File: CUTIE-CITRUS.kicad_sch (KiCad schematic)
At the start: 17 parts

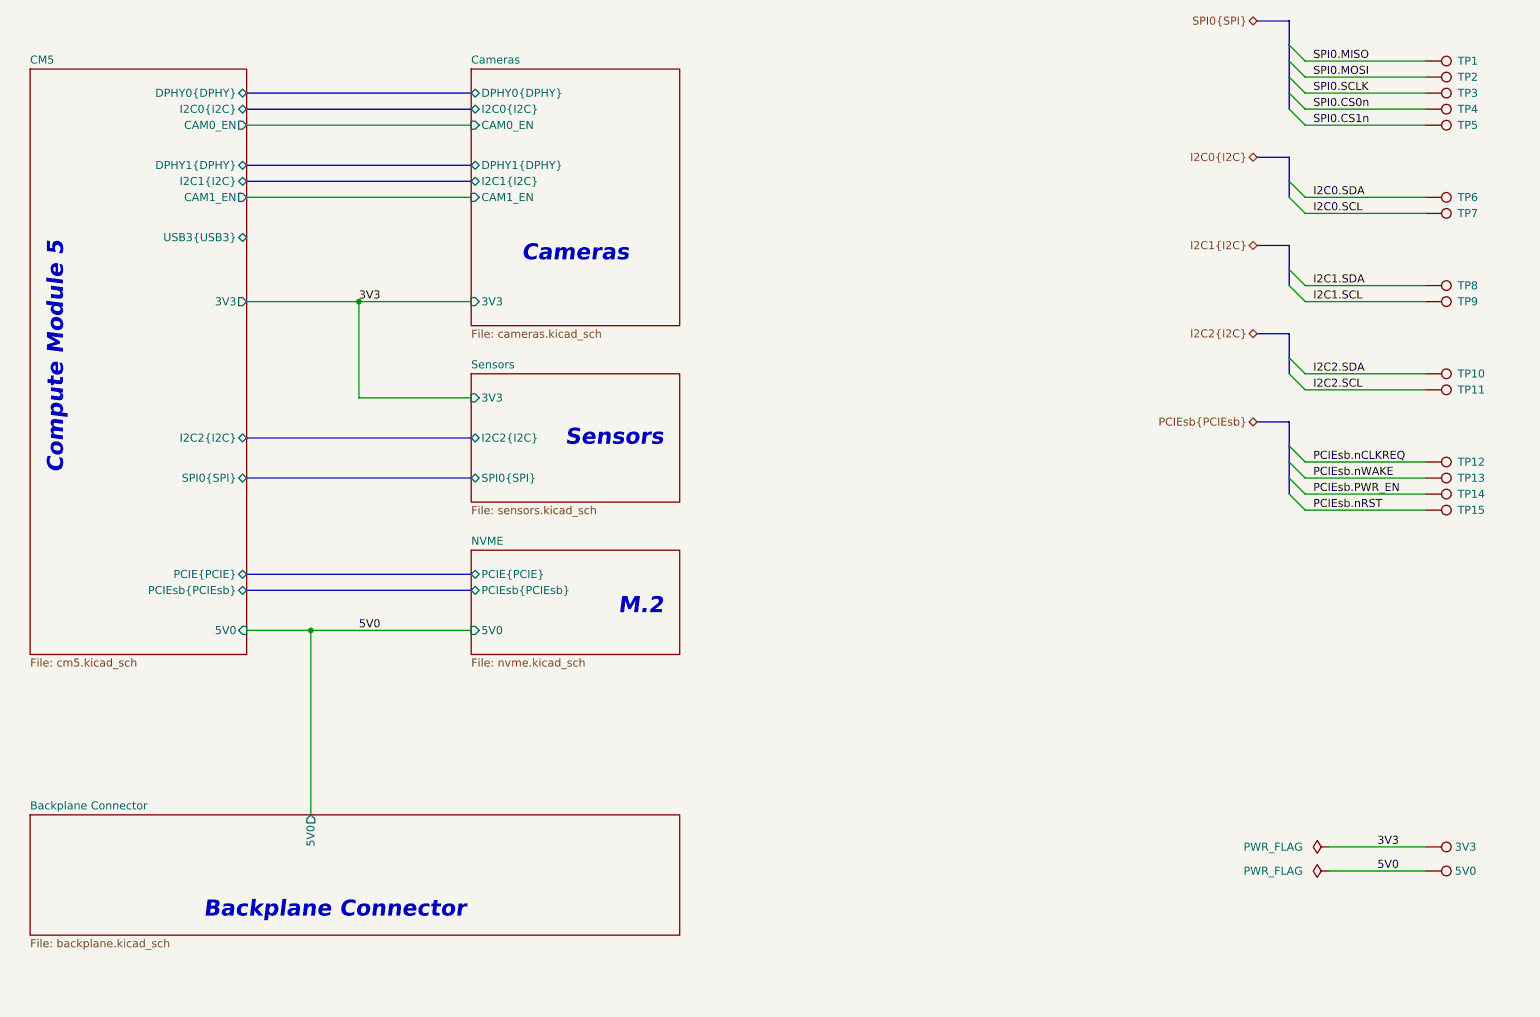
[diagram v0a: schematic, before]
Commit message: un-abstraction, footprints, layout edge cuts
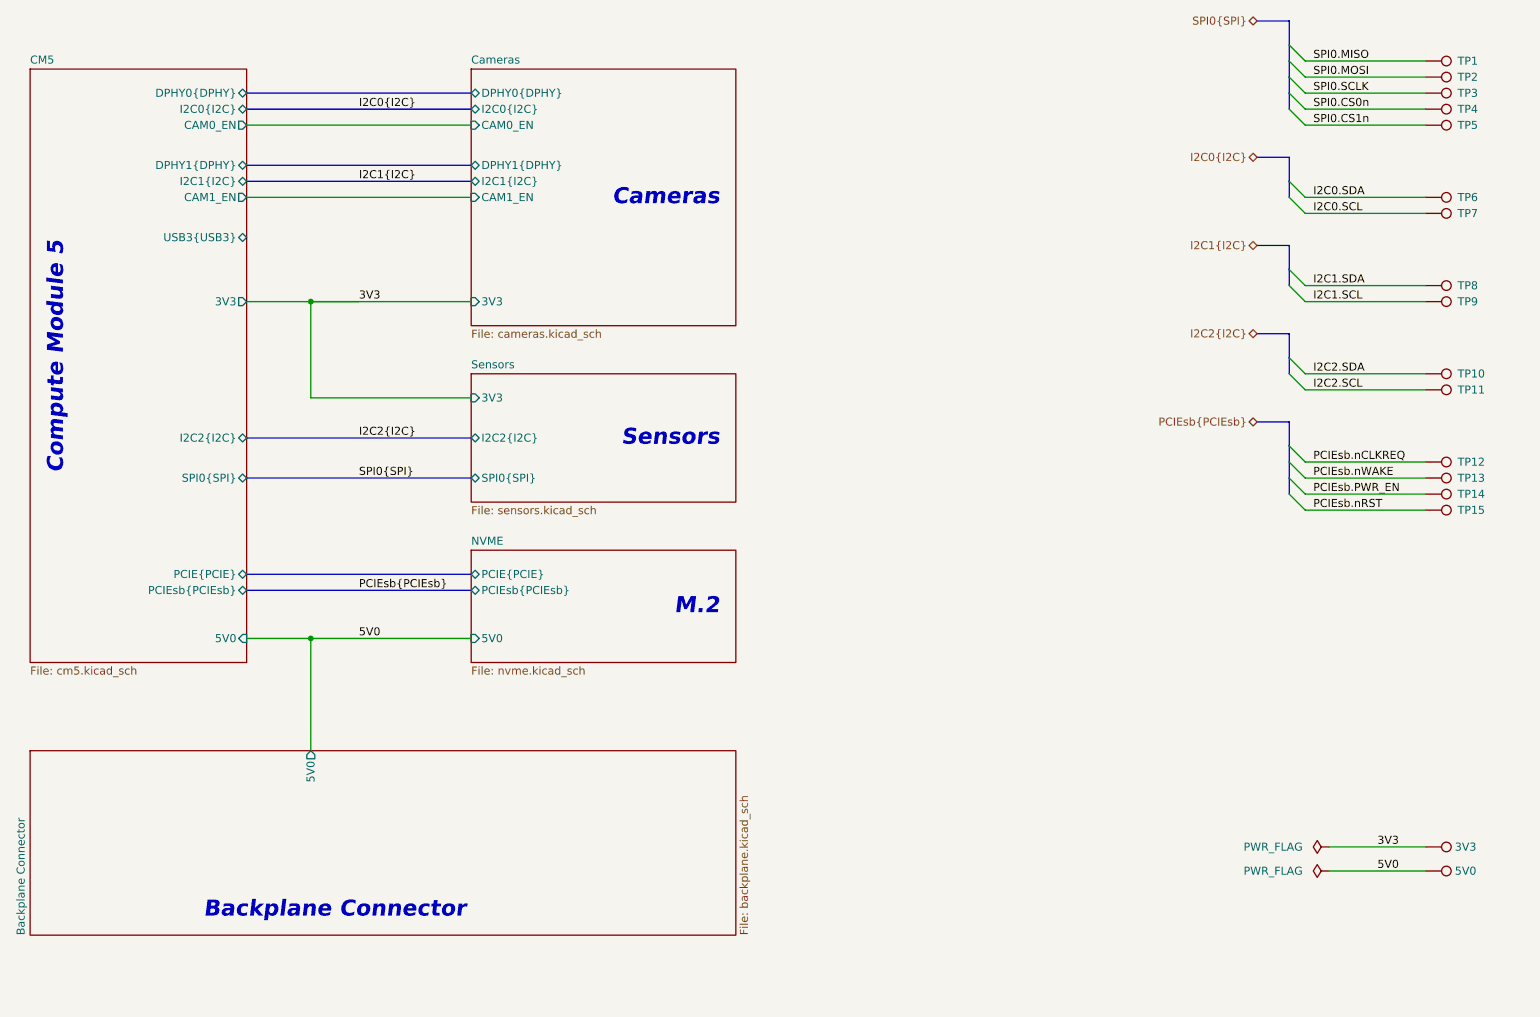
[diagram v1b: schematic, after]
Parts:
- 3V3, 5V0: footprint TestPoint:TestPoint_Pad_D1.0mm -> TestPoint:TestPoint_Pad_D2.0mm
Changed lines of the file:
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@@
 	(text "Cameras"
 		(exclude_from_sim no)
-		(at 129.54 62.23 0)
+		(at 152.4 53.34 0)
 		(effects
 			(font
@@
 				(color 0 0 0 1)
 			)
+			(justify right)
 		)
 	)
@@
 	(text "Sensors"
 		(exclude_from_sim no)
-		(at 143.51 91.44 0)
+		(at 152.4 91.44 0)
 		(effects
 			(font
@@
 	(text "M.2"
 		(exclude_from_sim no)
-		(at 143.51 118.11 0)
+		(at 152.4 118.11 0)
 		(effects
 			(font
@@
 	)
 	(junction
-		(at 95.25 69.85)
+		(at 87.63 69.85)
 		(diameter 0)
 		(color 255 153 0 1)
 	)
 	(junction
-		(at 87.63 121.92)
+		(at 87.63 123.19)
 		(diameter 0)
 		(color 255 0 0 1)
@@
 	(wire
 		(pts
-			(xy 95.25 85.09) (xy 113.03 85.09)
+			(xy 87.63 85.09) (xy 113.03 85.09)
 		)
 		(stroke
@@
 		)
 	)
+	(wire
+		(pts
+			(xy 87.63 123.19) (xy 113.03 123.19)
+		)
+		(stroke
+			(width 0.508)
+			(type default)
+			(color 255 0 0 1)
+		)
+	)
 	(bus
 		(pts
@@
 	(wire
 		(pts
-			(xy 87.63 121.92) (xy 113.03 121.92)
+			(xy 77.47 123.19) (xy 87.63 123.19)
 		)
 		(stroke
@@
 	(wire
 		(pts
+			(xy 87.63 123.19) (xy 87.63 140.97)
+		)
+		(stroke
+			(width 0.508)
+			(type default)
+			(color 255 0 0 1)
+		)
+	)
+	(wire
+		(pts
 			(xy 248.92 160.02) (xy 264.16 160.02)
 		)
@@
 	(wire
 		(pts
-			(xy 95.25 69.85) (xy 113.03 69.85)
+			(xy 77.47 69.85) (xy 87.63 69.85)
 		)
 		(stroke
@@
 	(wire
 		(pts
-			(xy 77.47 69.85) (xy 95.25 69.85)
+			(xy 87.63 69.85) (xy 113.03 69.85)
 		)
 		(stroke
@@
 	(wire
 		(pts
-			(xy 87.63 121.92) (xy 87.63 151.13)
-		)
-		(stroke
-			(width 0.508)
-			(type default)
-			(color 255 0 0 1)
+			(xy 245.11 97.79) (xy 264.16 97.79)
+		)
+		(stroke
+			(width 0)
+			(type default)
+		)
+	)
+	(bus
+		(pts
+			(xy 242.57 60.96) (xy 242.57 64.77)
+		)
+		(stroke
+			(width 0)
+			(type default)
+		)
+	)
+	(bus
+		(pts
+			(xy 237.49 25.4) (xy 242.57 25.4)
+		)
+		(stroke
+			(width 0)
+			(type default)
 		)
 	)
 	(wire
 		(pts
-			(xy 245.11 97.79) (xy 264.16 97.79)
-		)
-		(stroke
-			(width 0)
-			(type default)
-		)
-	)
-	(bus
-		(pts
-			(xy 242.57 60.96) (xy 242.57 64.77)
-		)
-		(stroke
-			(width 0)
-			(type default)
-		)
-	)
-	(bus
-		(pts
-			(xy 237.49 25.4) (xy 242.57 25.4)
+			(xy 245.11 69.85) (xy 264.16 69.85)
 		)
 		(stroke
@@
 	(wire
 		(pts
-			(xy 245.11 69.85) (xy 264.16 69.85)
+			(xy 95.25 69.85) (xy 87.63 69.85)
 		)
 		(stroke
@@
 		)
 	)
+	(bus
+		(pts
+			(xy 77.47 48.26) (xy 113.03 48.26)
+		)
+		(stroke
+			(width 0)
+			(type default)
+		)
+	)
 	(wire
 		(pts
-			(xy 77.47 121.92) (xy 87.63 121.92)
-		)
-		(stroke
-			(width 0.508)
-			(type default)
-			(color 255 0 0 1)
-		)
-	)
-	(bus
-		(pts
-			(xy 77.47 48.26) (xy 113.03 48.26)
-		)
-		(stroke
-			(width 0)
-			(type default)
-		)
-	)
-	(wire
-		(pts
-			(xy 95.25 69.85) (xy 95.25 85.09)
+			(xy 87.63 69.85) (xy 87.63 85.09)
 		)
 		(stroke
@@
 		)
 	)
+	(label "I2C1{I2C}"
+		(at 95.25 50.8 0)
+		(effects
+			(font
+				(size 1.27 1.27)
+			)
+			(justify bottom)
+		)
+	)
 	(label "SPI0.SCLK"
 		(at 246.38 36.83 0)
@@
 		)
 	)
+	(label "SPI0{SPI}"
+		(at 95.25 97.79 0)
+		(effects
+			(font
+				(size 1.27 1.27)
+			)
+			(justify bottom)
+		)
+	)
 	(label "I2C1.SDA"
 		(at 246.38 67.31 0)
@@
 	)
 	(label "5V0"
-		(at 95.25 121.92 0)
+		(at 95.25 123.19 0)
 		(effects
 			(font
@@
 		)
 	)
+	(label "PCIEsb{PCIEsb}"
+		(at 95.25 115.57 0)
+		(effects
+			(font
+				(size 1.27 1.27)
+			)
+			(justify bottom)
+		)
+	)
 	(label "PCIEsb.PWR_EN"
 		(at 246.38 100.33 0)
@@
 		)
 	)
+	(label "I2C2{I2C}"
+		(at 95.25 91.44 0)
+		(effects
+			(font
+				(size 1.27 1.27)
+			)
+			(justify bottom)
+		)
+	)
 	(label "3V3"
 		(at 256.54 156.21 0)
+		(effects
+			(font
+				(size 1.27 1.27)
+			)
+			(justify bottom)
+		)
+	)
+	(label "I2C0{I2C}"
+		(at 95.25 39.37 0)
 		(effects
 			(font
@@
 			)
 		)
-		(property "Footprint" "TestPoint:TestPoint_Pad_D1.0mm"
+		(property "Footprint" "TestPoint:TestPoint_Pad_D2.0mm"
 			(at 264.16 161.29 0)
 			(effects
@@
 			)
 		)
-		(property "Footprint" "TestPoint:TestPoint_Pad_D1.0mm"
+		(property "Footprint" "TestPoint:TestPoint_Pad_D2.0mm"
 			(at 264.16 165.1 0)
 			(effects
@@
 	(sheet
 		(at 43.18 33.02)
-		(size 34.29 92.71)
+		(size 34.29 93.98)
 		(exclude_from_sim no)
 		(in_bom yes)
@@
 		)
 		(property "Sheetfile" "cm5.kicad_sch"
-			(at 43.18 126.3146 0)
+			(at 43.18 127.5846 0)
 			(effects
 				(font
@@
 		)
 		(pin "5V0" input
-			(at 77.47 121.92 0)
+			(at 77.47 123.19 0)
 			(effects
 				(font
@@
 	(sheet
 		(at 113.03 33.02)
-		(size 33.02 40.64)
+		(size 41.91 40.64)
 		(exclude_from_sim no)
 		(in_bom yes)
@@
 	(sheet
 		(at 113.03 81.28)
-		(size 33.02 20.32)
+		(size 41.91 20.32)
 		(exclude_from_sim no)
 		(in_bom yes)
@@
 	(sheet
 		(at 113.03 109.22)
-		(size 33.02 16.51)
+		(size 41.91 17.78)
 		(exclude_from_sim no)
 		(in_bom yes)
@@
 		)
 		(property "Sheetfile" "nvme.kicad_sch"
-			(at 113.03 126.3146 0)
+			(at 113.03 127.5846 0)
 			(effects
 				(font
@@
 		)
 		(pin "5V0" input
-			(at 113.03 121.92 180)
+			(at 113.03 123.19 180)
 			(effects
 				(font
@@
 	)
 	(sheet
-		(at 43.18 151.13)
-		(size 102.87 19.05)
+		(at 43.18 140.97)
+		(size 111.76 29.21)
 		(exclude_from_sim no)
 		(in_bom yes)
@@
 		)
 		(property "Sheetname" "Backplane Connector"
-			(at 43.18 150.4184 0)
+			(at 42.4684 170.18 90)
 			(effects
 				(font
@@
 		)
 		(property "Sheetfile" "backplane.kicad_sch"
-			(at 43.18 170.7646 0)
+			(at 155.5246 170.18 90)
 			(effects
 				(font
@@
 		)
 		(pin "5V0" output
-			(at 87.63 151.13 90)
-			(effects
-				(font
+			(at 87.63 140.97 90)
+			(effects
+				(font

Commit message: moved TPs
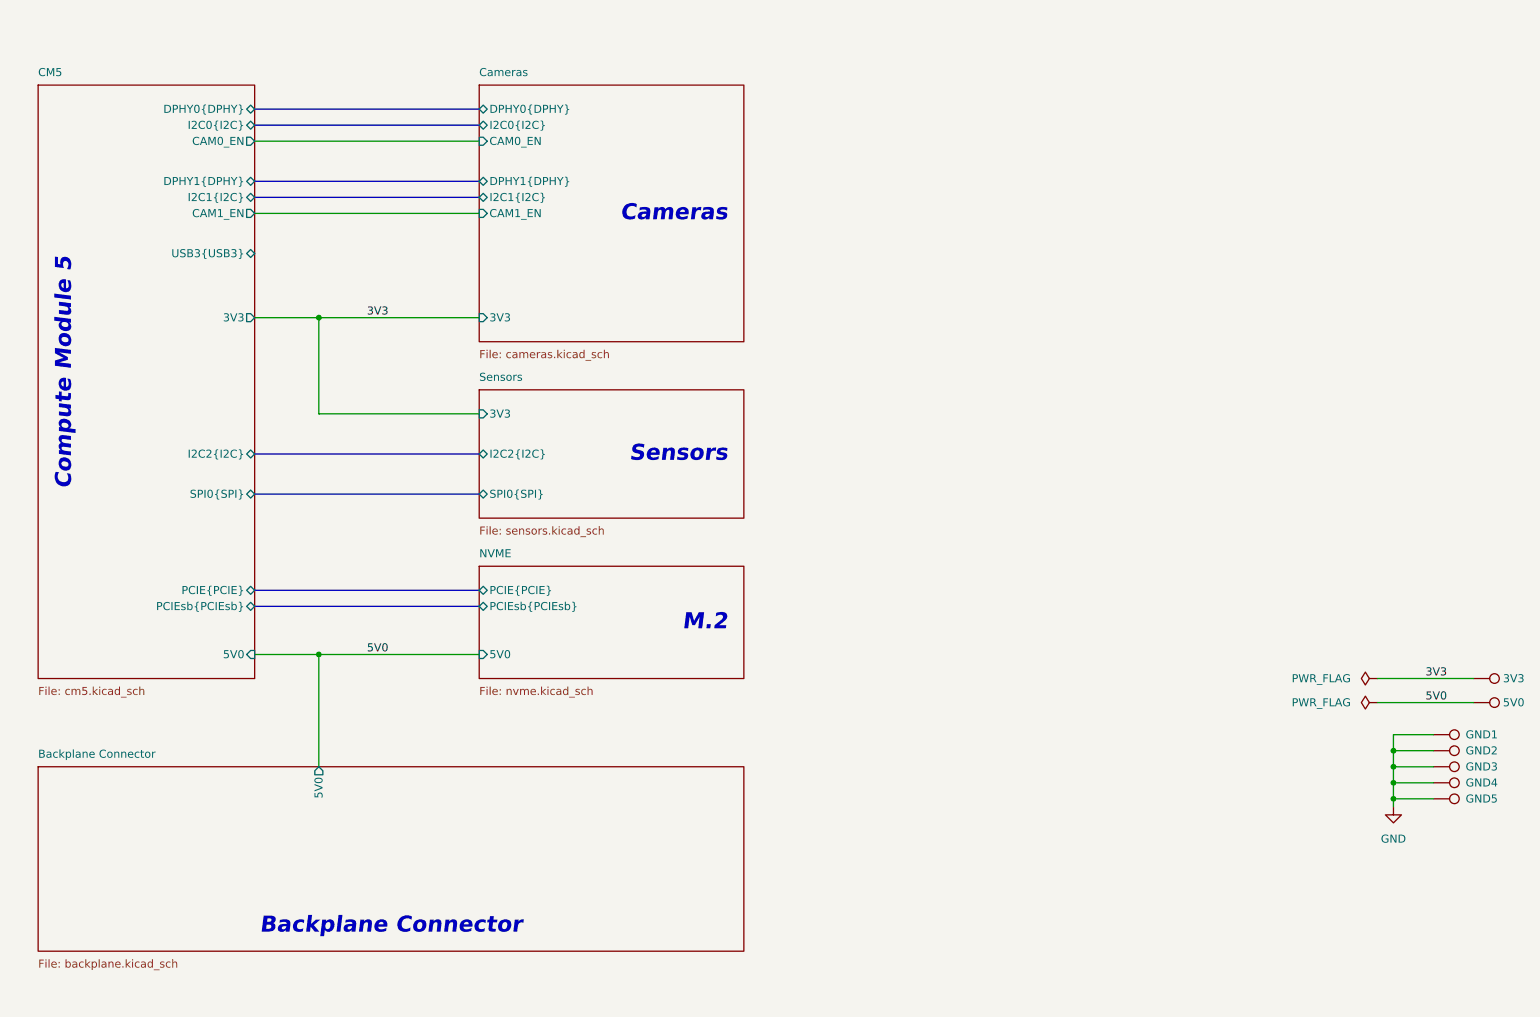
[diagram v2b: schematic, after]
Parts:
- removed TP1, TP10, TP11, TP12, TP13, TP14, TP15, TP2, TP3, TP4, TP5, TP6, TP7, TP8, TP9: TestPoint, TestPoint:TestPoint_Pad_D1.0mm, symbol Connector:TestPoint
- added GND1, GND2, GND3, GND4, GND5: TestPoint, TestPoint:TestPoint_Pad_D1.0mm, symbol Connector:TestPoint
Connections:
- new net GND: GND1.1, GND2.1, GND3.1, GND4.1, GND5.1
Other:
- moved on the sheet: 3V3, 5V0

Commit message: moved power TPs to cm5 sheet
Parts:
- removed 3V3, 5V0: TestPoint, TestPoint:TestPoint_Pad_D2.0mm, symbol Connector:TestPoint
- removed GND1, GND2, GND3, GND4, GND5: TestPoint, TestPoint:TestPoint_Pad_D1.0mm, symbol Connector:TestPoint

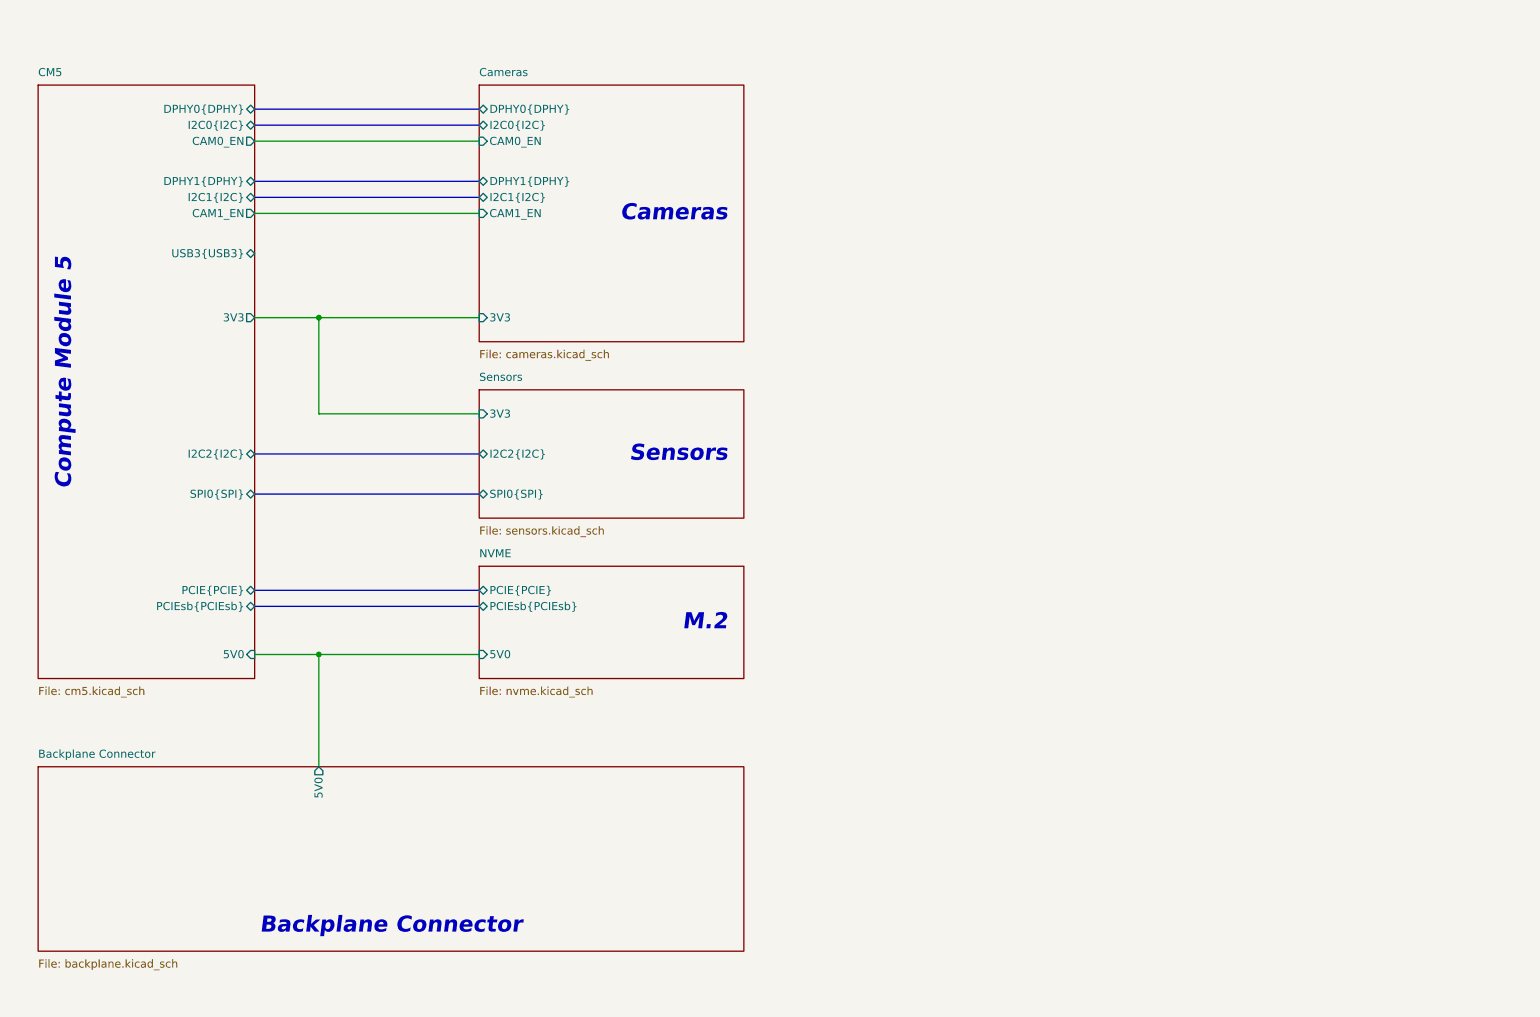
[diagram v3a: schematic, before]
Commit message: added conns to backplane
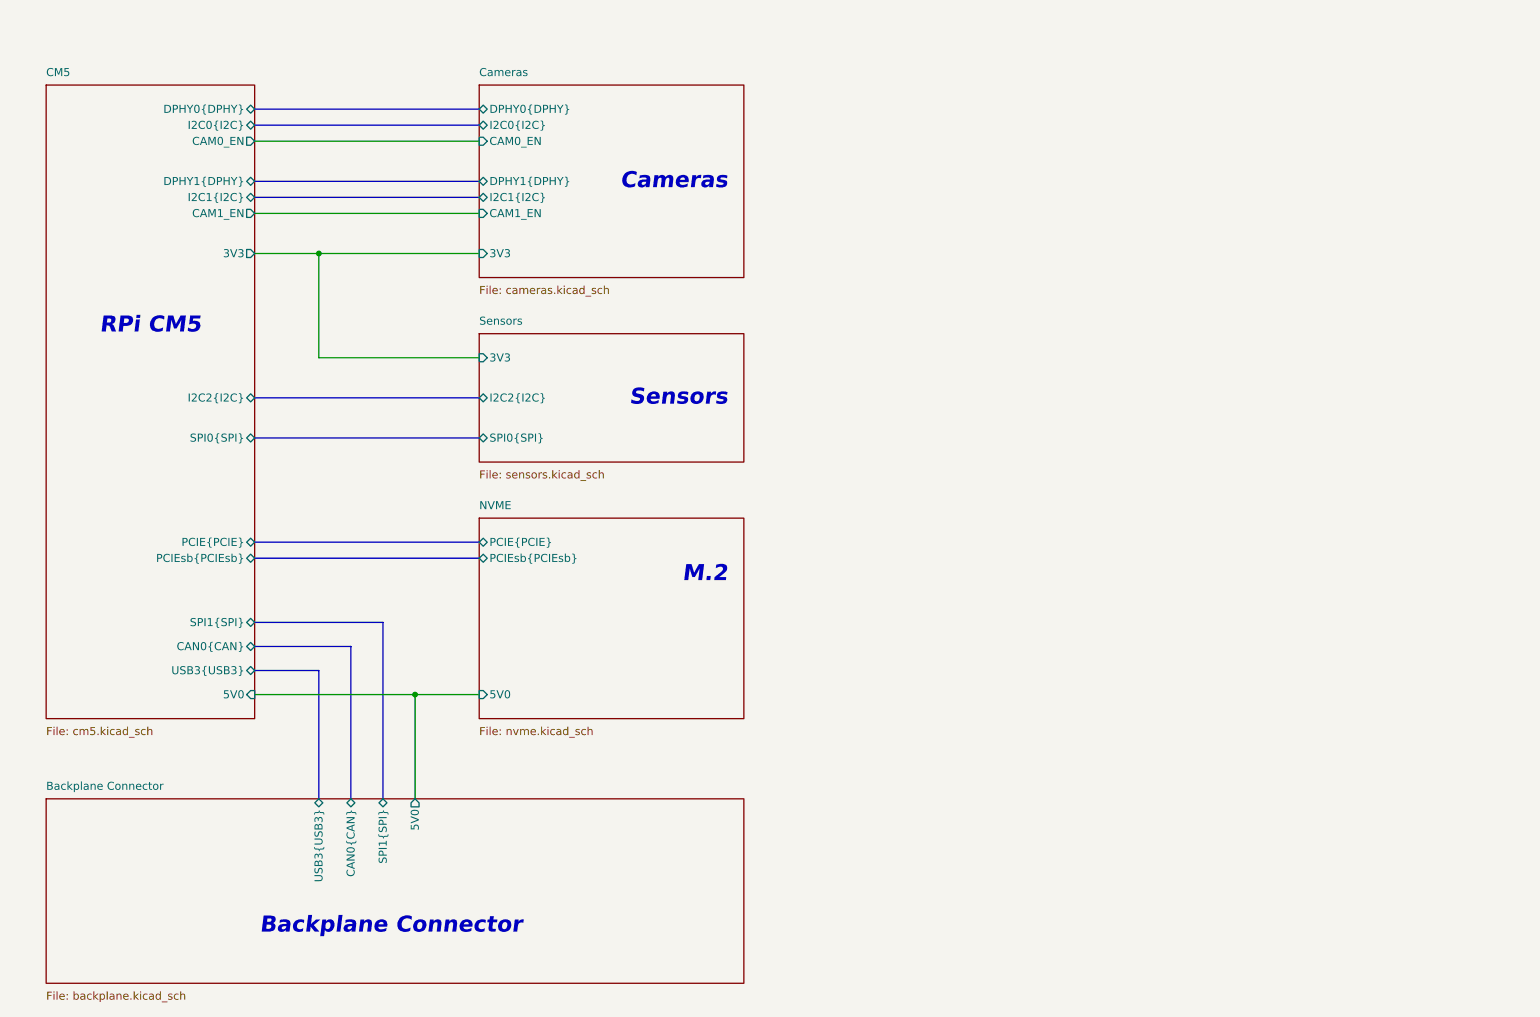
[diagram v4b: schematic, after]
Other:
- sheet Backplane Connector ports: added CAN0{CAN}, SPI1{SPI}, USB3{USB3}; removed none
- sheet CM5 ports: added CAN0{CAN}, SPI1{SPI}; removed none
- note added: "RPi CM5"
- note removed: "Compute Module 5"
